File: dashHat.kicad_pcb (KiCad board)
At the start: 4 copper layers, 65 x 56 mm, 155 parts, among them J1 Input, J2 LCD, J3 GPIO, J4 LEDs, J5 Ride Through, J6 SMA, J7 Conn_01x08, Q1 BSS138, Q10 ADP197, Q12 BSS138, Q2 BSS138, Q3 2N7002, Q4 BSS84, Q5 BSS84, Q6 BSS84, Q7 , Q8 , Q9 BSS84, U1 CAT24C256, U12 MAX22193, U13 IX4427, U2 MAX17614, U3 TVS3300DRV, U4 LM61480, U5 74LVC1G80, U6 ZOE-M8Q, U7 TCAN330, U8 MCP2515-xST, U9 MAX3227, Y1 32.768k, Y2 8MHz

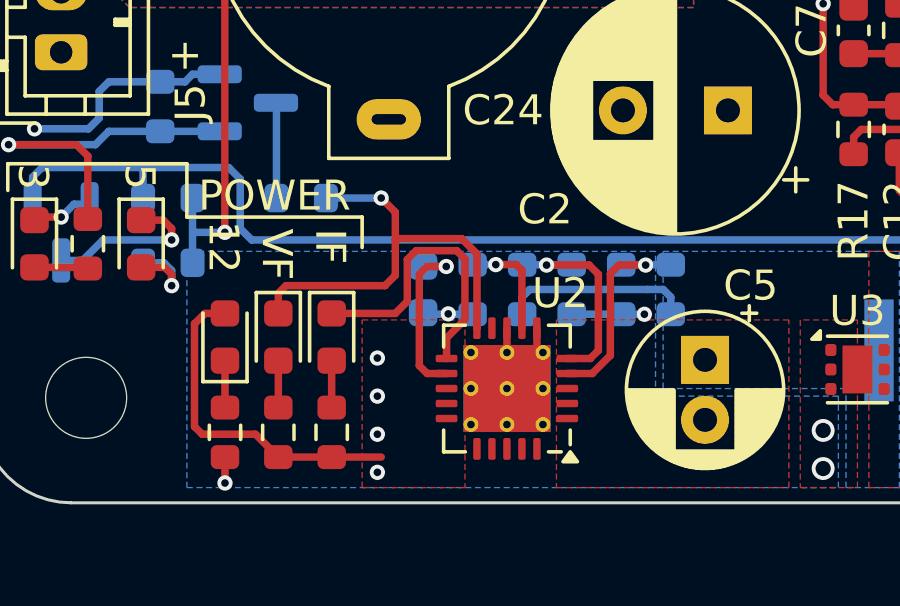
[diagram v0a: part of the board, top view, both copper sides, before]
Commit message: selectable current limit mode
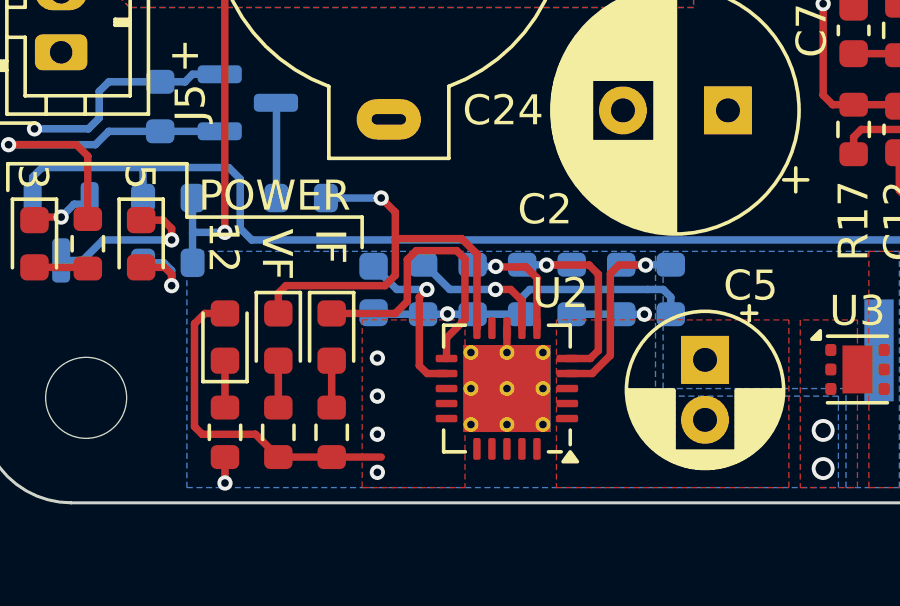
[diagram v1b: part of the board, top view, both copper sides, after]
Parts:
- added R48: 0, Resistor_SMD:R_0603_1608Metric, B.Cu at (116.4, 92.9)
- moved C6 1.65 mm to (113.1, 92.9)
- moved R15 1.65 mm to (114.7, 92.9)
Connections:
- U2 pad 6: GND -> Net-(U2-CLMODE)
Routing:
- net Net-(U2-CLMODE): track 0.00 -> 4.01 mm, vias 0 -> 1
- net GND: track 98.7 -> 101.0 mm
- net Net-(U2-SETI): track 3.65 -> 4.71 mm

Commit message: fix up silkscreen
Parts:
- moved C23 0.40 mm to (120.7, 74.9)
- moved L3 0.25 mm to (120.6, 72.8)
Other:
- board text added: "PI"

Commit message: switch can crystal to 12MHz
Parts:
- Y2: value 8MHz -> 12MHz
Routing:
- net GND: vias 122 -> 130
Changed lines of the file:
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@@
 		(tags "SMA")
 		(property "Reference" "J6"
-			(at -3.81 -4.826 0)
+			(at -3.81 -5.461 0)
 			(layer "F.SilkS")
 			(effects
@@
 		(tags "SOT TO_SOT_SMD")
 		(property "Reference" "Q12"
-			(at 0 -2.54 360)
+			(at 0 -2.54 0)
 			(layer "B.SilkS")
 			(effects
@@
 		)
 		(property "Value" "BSS138"
-			(at 0 -2.4 360)
+			(at 0 -2.4 0)
 			(layer "B.Fab")
 			(effects
@@
 		)
 		(fp_text user "${REFERENCE}"
-			(at 0 0 360)
+			(at 0 0 0)
 			(layer "B.Fab")
 			(effects
@@
 			)
 		)
-		(property "Value" "8MHz"
+		(property "Value" "12MHz"
 			(at 0 -2.45 180)
 			(layer "B.Fab")
@@
 			)
 		)
-		(property "Mfg Part Number" "FL0800008Q"
+		(property "Mfg Part Number" "FL1200112"
 			(at 0 0 0)
 			(unlocked yes)
@@
 	)
 	(via
+		(at 106.604 74.981)
+		(size 0.508)
+		(drill 0.254)
+		(layers "F.Cu" "B.Cu")
+		(free yes)
+		(net 1)
+	)
+	(via
 		(at 108.128 99.3396)
 		(size 0.508)
@@
 	)
 	(via
+		(at 106.604 73.33)
+		(size 0.508)
+		(drill 0.254)
+		(layers "F.Cu" "B.Cu")
+		(free yes)
+		(net 1)
+	)
+	(via
 		(at 124.638 74.219)
 		(size 0.508)
@@
 	)
 	(via
+		(at 110.795 69.901)
+		(size 0.508)
+		(drill 0.254)
+		(layers "F.Cu" "B.Cu")
+		(free yes)
+		(net 1)
+	)
+	(via
 		(at 143.434 78.791)
 		(size 0.508)
@@
 	)
 	(via
+		(at 105.207 61.011)
+		(size 0.508)
+		(drill 0.254)
+		(layers "F.Cu" "B.Cu")
+		(free yes)
+		(net 1)
+	)
+	(via
 		(at 132.131 66.472)
 		(size 0.508)
@@
 	)
 	(via
+		(at 107.239 61.011)
+		(size 0.508)
+		(drill 0.254)
+		(layers "F.Cu" "B.Cu")
+		(free yes)
+		(net 1)
+	)
+	(via
 		(at 135.179 66.472)
 		(size 0.508)
@@
 	)
 	(via
+		(at 109.144 61.011)
+		(size 0.508)
+		(drill 0.254)
+		(layers "F.Cu" "B.Cu")
+		(free yes)
+		(net 1)
+	)
+	(via
 		(at 118.542 67.488)
 		(size 0.508)
@@
 	)
 	(via
+		(at 107.874 71.425)
+		(size 0.508)
+		(drill 0.254)
+		(layers "F.Cu" "B.Cu")
+		(free yes)
+		(net 1)
+	)
+	(via
 		(at 158.547 84.76)
 		(size 0.508)
@@
 		(size 0.508)
 		(drill 0.254)
+		(layers "F.Cu" "B.Cu")
+		(free yes)
+		(net 1)
+	)
+	(via
+		(at 109.144 62.535)
+		(size 0.508)
+		(drill 0.254)
